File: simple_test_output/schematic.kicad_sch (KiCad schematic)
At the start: 4 parts, among them U1 STM32F103C8T6, U2 LTR303A1R, U3 CP2102N-A01-GQ, U4 LM1117-3.3

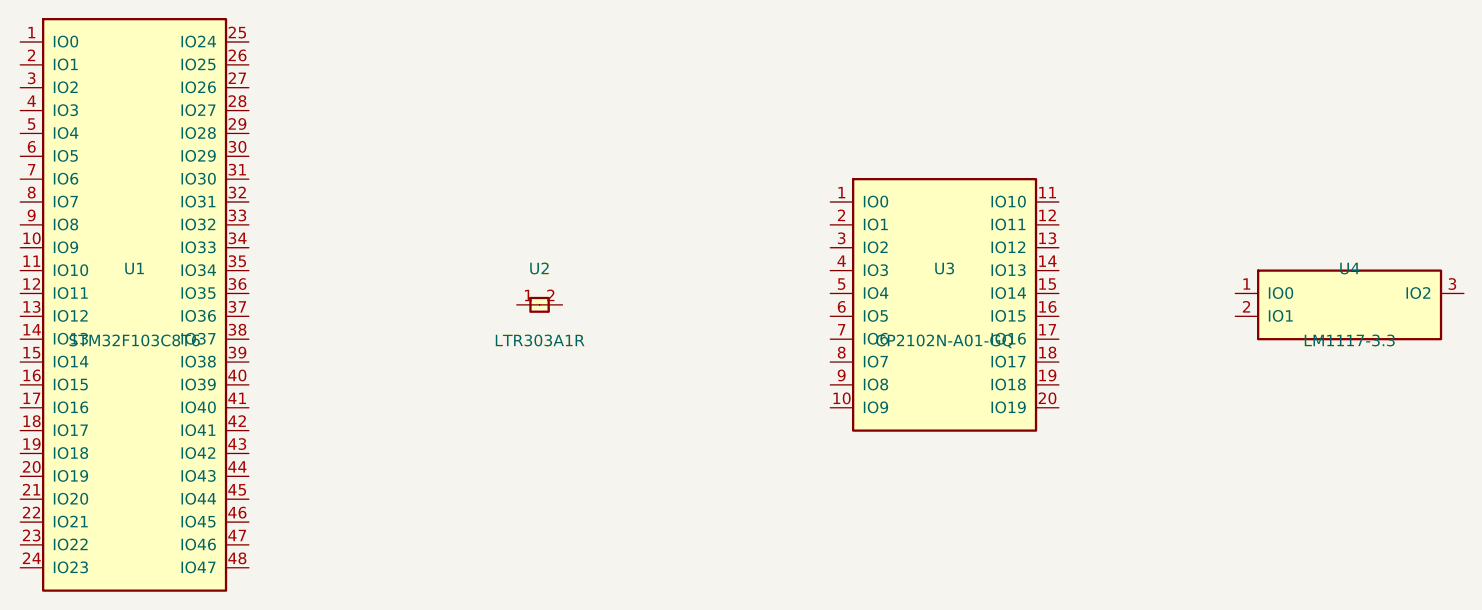
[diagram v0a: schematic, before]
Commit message: chore: add test outputs to .gitignore
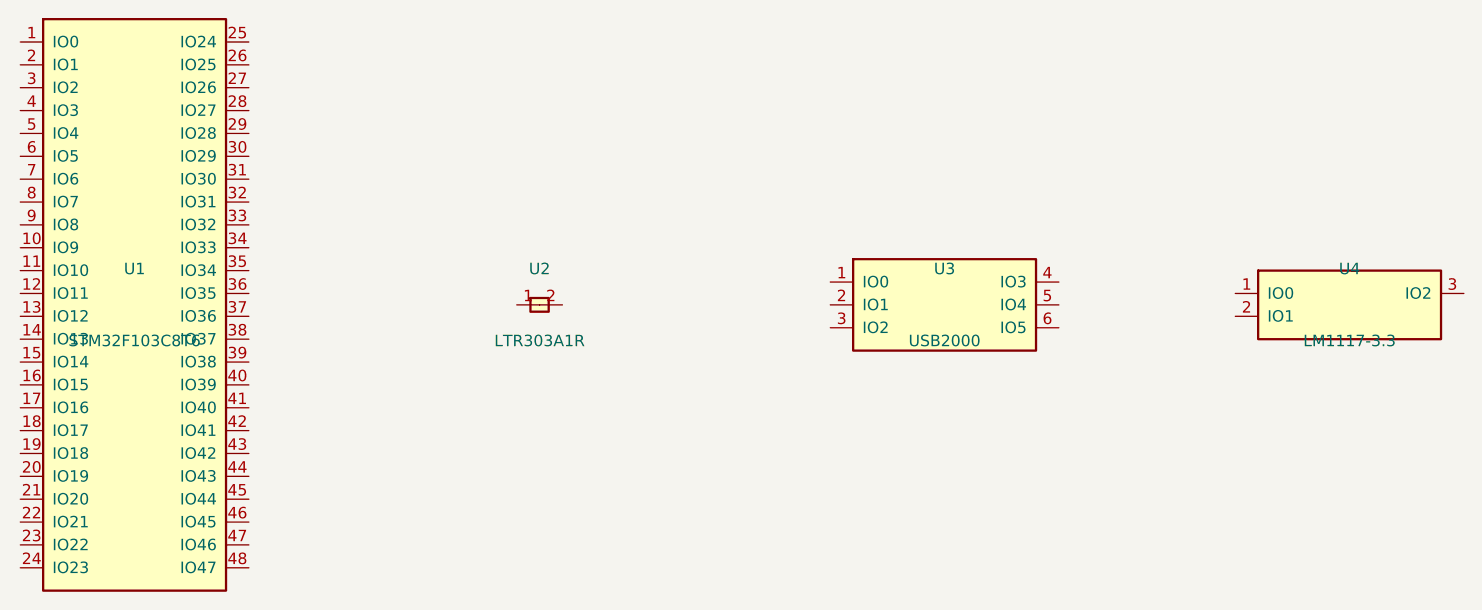
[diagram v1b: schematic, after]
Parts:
- removed U3: CP2102N-A01-GQ, pcbai:SSOP-20, symbol pcbai:SSOP-20
- removed U4: LM1117-3.3, Package_TO_SOT_SMD:SOT-223-3_TabPin2, symbol pcbai:SOT-223
- added U3: USB2000, pcbai:SOT-23-6, symbol pcbai:SOT-23-6
- added U4: LM1117-3.3, pcbai:TO-220, symbol pcbai:TO-220
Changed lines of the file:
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@@
     )
   )
-  (symbol (lib_id "pcbai:SSOP-20") (at 120.0 30.0 0)
+  (symbol (lib_id "pcbai:SOT-23-6") (at 120.0 30.0 0)
     (unit 1)
     (in_bom yes) (on_board yes) (dnp no)
@@
       (effects (font (size 1.27 1.27)))
     )
-    (property "Value" "CP2102N-A01-GQ" (at 120.0 34.0 0)
+    (property "Value" "USB2000" (at 120.0 34.0 0)
       (effects (font (size 1.27 1.27)))
     )
-    (property "Footprint" "pcbai:SSOP-20" (at 120.0 30.0 0)
+    (property "Footprint" "pcbai:SOT-23-6" (at 120.0 30.0 0)
       (effects (font (size 1.27 1.27)) hide)
     )
@@
     )
   )
-  (symbol (lib_id "pcbai:SOT-223") (at 165.0 30.0 0)
+  (symbol (lib_id "pcbai:TO-220") (at 165.0 30.0 0)
     (unit 1)
     (in_bom yes) (on_board yes) (dnp no)
@@
       (effects (font (size 1.27 1.27)))
     )
-    (property "Footprint" "Package_TO_SOT_SMD:SOT-223-3_TabPin2" (at 165.0 30.0 0)
+    (property "Footprint" "pcbai:TO-220" (at 165.0 30.0 0)
       (effects (font (size 1.27 1.27)) hide)
     )
